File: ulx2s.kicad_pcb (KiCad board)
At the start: 4 copper layers, 35.6 x 61 mm, 23 parts, among them J1 Conn_01x24, J2 Conn_01x24, J3 Micro_SD_Card_Det, J4 USB_OTG, J5 Conn_01x06, SW1 SW_Push, SW2 SW_Push, SW3 SW_Push, SW4 SW_Push, SW5 SW_Push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

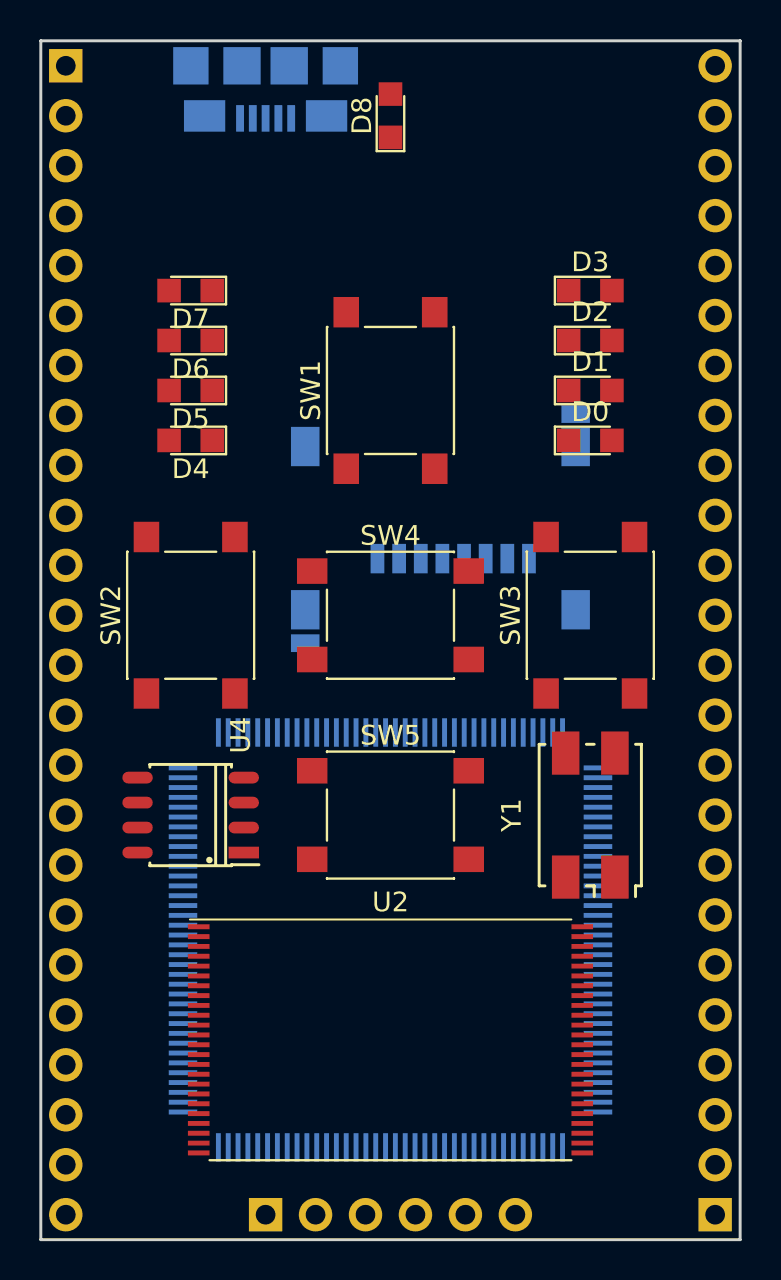
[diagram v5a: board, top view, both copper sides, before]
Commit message: usbserial chip ft232rl
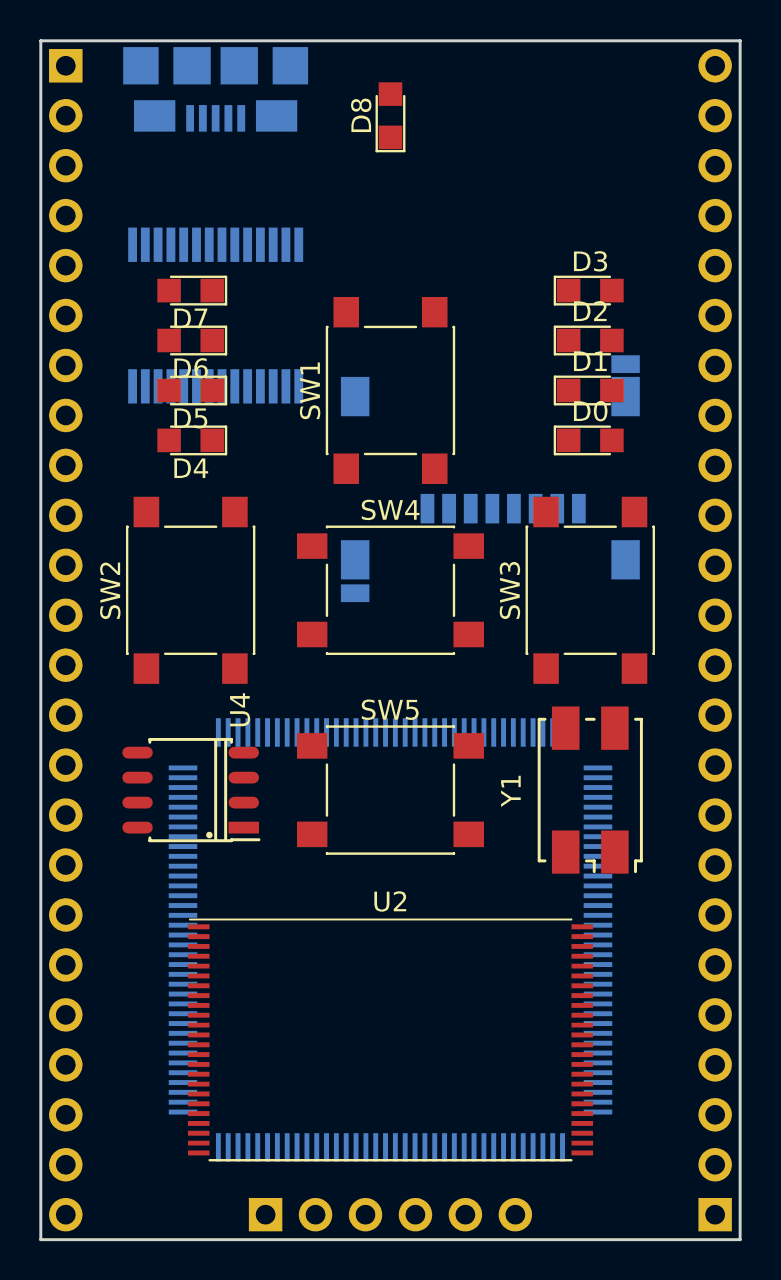
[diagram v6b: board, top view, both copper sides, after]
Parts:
- added U3: FT232RL, Housings_SSOP:SSOP-28_5.3x10.2mm_Pitch0.65mm, B.Cu at (149.9, 95.2)
- moved J3 3.59 mm to (163.8, 102.9)
- moved J4 2.54 mm to (149.9, 82.5)
- moved SW5 1.27 mm to (158.8, 119.4)
- moved U4 1.27 mm to (148.6, 119.4)
- moved Y1 1.27 mm to (168.9, 119.4)
- moved SW2 1.27 mm to (148.6, 109.2)
- moved SW3 1.27 mm to (168.9, 109.2)
- moved SW4 1.27 mm to (158.8, 109.2)
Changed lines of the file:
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@@
     (tracks 0)
     (zones 0)
-    (modules 23)
+    (modules 24)
     (nets 13)
   )
@@
   (layers
     (0 F.Cu signal)
-    (1 In1.Cu signal)
-    (2 In2.Cu signal)
-    (31 B.Cu signal)
+    (1 In1.Cu signal hide)
+    (2 In2.Cu signal hide)
+    (31 B.Cu signal hide)
     (32 B.Adhes user)
     (33 F.Adhes user)
@@
   )
   (module micro-sd:SCHD3A100 (layer B.Cu)
-    (at 161.29 105.41 270)
+    (at 163.83 102.87 270)
     (descr "Micro SD card slot SCHD3A0100 from ALPS or ON-STARS")
     (tags "Micro SD SCHD3A0100")
@@
   )
   (module usb_otg:USB-MICRO-B-FCI-10118192-0001LF (layer B.Cu)
-    (at 152.4 82.55)
+    (at 149.86 82.55)
     (fp_text reference J4 (at 0 4.2) (layer B.SilkS)
       (effects (font (size 0.7 0.7) (thickness 0.15)) (justify mirror))
@@
   )
   (module oscxo:Crystal_SMD_7050_4Pads (layer F.Cu)
-    (at 168.91 120.65 90)
+    (at 168.91 119.38 90)
     (descr "Crystal oscillator, 7.0x5.0mm, 4 Pads")
     (tags "crystal oscillator quartz SMD SMT 7050")
@@
   )
   (module Buttons_Switches_SMD:SW_SPST_PTS645 (layer F.Cu)
-    (at 148.59 110.49 90)
+    (at 148.59 109.22 90)
     (descr "C&K Components SPST SMD PTS645 Series 6mm Tact Switch")
     (tags "SPST Button Switch")
@@
   )
   (module Buttons_Switches_SMD:SW_SPST_PTS645 (layer F.Cu)
-    (at 168.91 110.49 90)
+    (at 168.91 109.22 90)
     (descr "C&K Components SPST SMD PTS645 Series 6mm Tact Switch")
     (tags "SPST Button Switch")
@@
   )
   (module Buttons_Switches_SMD:SW_SPST_PTS645 (layer F.Cu)
-    (at 158.75 110.49)
+    (at 158.75 109.22)
     (descr "C&K Components SPST SMD PTS645 Series 6mm Tact Switch")
     (tags "SPST Button Switch")
@@
   )
   (module Buttons_Switches_SMD:SW_SPST_PTS645 (layer F.Cu)
-    (at 158.75 120.65)
+    (at 158.75 119.38)
     (descr "C&K Components SPST SMD PTS645 Series 6mm Tact Switch")
     (tags "SPST Button Switch")
@@
   )
   (module SOA008-150mil:SOA008-150mil (layer F.Cu)
-    (at 148.59 120.65 180)
+    (at 148.59 119.38 180)
     (descr "Cypress SOA008 SOIC-8 150 mil")
     (tags "SOA008 SOIC-8 1.27 150 mil")
@@
       (at (xyz 0 0 0))
       (scale (xyz 1 1 1))
+      (rotate (xyz 0 0 0))
+    )
+  )
+  (module Housings_SSOP:SSOP-28_5.3x10.2mm_Pitch0.65mm (layer B.Cu)
+    (at 149.86 95.25 90)
+    (descr "28-Lead Plastic Shrink Small Outline (SS)-5.30 mm Body [SSOP] (see Microchip Packaging Specification 00000049BS.pdf)")
+    (tags "SSOP 0.65")
+    (attr smd)
+    (fp_text reference U3 (at 0 6.25 90) (layer B.SilkS)
+      (effects (font (size 1 1) (thickness 0.15)) (justify mirror))
+    )
+    (fp_text value FT232RL (at 0 -6.25 90) (layer B.Fab)
+      (effects (font (size 1 1) (thickness 0.15)) (justify mirror))
+    )
+    (fp_line (start -1.65 5.1) (end 2.65 5.1) (layer B.Fab) (width 0.15))
+    (fp_line (start 2.65 5.1) (end 2.65 -5.1) (layer B.Fab) (width 0.15))
+    (fp_line (start 2.65 -5.1) (end -2.65 -5.1) (layer B.Fab) (width 0.15))
+    (fp_line (start -2.65 -5.1) (end -2.65 4.1) (layer B.Fab) (width 0.15))
+    (fp_line (start -2.65 4.1) (end -1.65 5.1) (layer B.Fab) (width 0.15))
+    (fp_line (start -4.75 5.5) (end -4.75 -5.5) (layer B.CrtYd) (width 0.05))
+    (fp_line (start 4.75 5.5) (end 4.75 -5.5) (layer B.CrtYd) (width 0.05))
+    (fp_line (start -4.75 5.5) (end 4.75 5.5) (layer B.CrtYd) (width 0.05))
+    (fp_line (start -4.75 -5.5) (end 4.75 -5.5) (layer B.CrtYd) (width 0.05))
+    (fp_line (start -2.875 5.325) (end -2.875 4.75) (layer B.SilkS) (width 0.15))
+    (fp_line (start 2.875 5.325) (end 2.875 4.675) (layer B.SilkS) (width 0.15))
+    (fp_line (start 2.875 -5.325) (end 2.875 -4.675) (layer B.SilkS) (width 0.15))
+    (fp_line (start -2.875 -5.325) (end -2.875 -4.675) (layer B.SilkS) (width 0.15))
+    (fp_line (start -2.875 5.325) (end 2.875 5.325) (layer B.SilkS) (width 0.15))
+    (fp_line (start -2.875 -5.325) (end 2.875 -5.325) (layer B.SilkS) (width 0.15))
+    (fp_line (start -2.875 4.75) (end -4.475 4.75) (layer B.SilkS) (width 0.15))
+    (fp_text user %R (at 0 0 90) (layer B.Fab)
+      (effects (font (size 0.8 0.8) (thickness 0.15)) (justify mirror))
+    )
+    (pad 1 smd rect (at -3.6 4.225 90) (size 1.75 0.45) (layers B.Cu B.Paste B.Mask))
+    (pad 2 smd rect (at -3.6 3.575 90) (size 1.75 0.45) (layers B.Cu B.Paste B.Mask))
+    (pad 3 smd rect (at -3.6 2.925 90) (size 1.75 0.45) (layers B.Cu B.Paste B.Mask))
+    (pad 4 smd rect (at -3.6 2.275 90) (size 1.75 0.45) (layers B.Cu B.Paste B.Mask))
+    (pad 5 smd rect (at -3.6 1.625 90) (size 1.75 0.45) (layers B.Cu B.Paste B.Mask))
+    (pad 6 smd rect (at -3.6 0.975 90) (size 1.75 0.45) (layers B.Cu B.Paste B.Mask))
+    (pad 7 smd rect (at -3.6 0.325 90) (size 1.75 0.45) (layers B.Cu B.Paste B.Mask))
+    (pad 8 smd rect (at -3.6 -0.325 90) (size 1.75 0.45) (layers B.Cu B.Paste B.Mask))
+    (pad 9 smd rect (at -3.6 -0.975 90) (size 1.75 0.45) (layers B.Cu B.Paste B.Mask))
+    (pad 10 smd rect (at -3.6 -1.625 90) (size 1.75 0.45) (layers B.Cu B.Paste B.Mask))
+    (pad 11 smd rect (at -3.6 -2.275 90) (size 1.75 0.45) (layers B.Cu B.Paste B.Mask))
+    (pad 12 smd rect (at -3.6 -2.925 90) (size 1.75 0.45) (layers B.Cu B.Paste B.Mask))
+    (pad 13 smd rect (at -3.6 -3.575 90) (size 1.75 0.45) (layers B.Cu B.Paste B.Mask))
+    (pad 14 smd rect (at -3.6 -4.225 90) (size 1.75 0.45) (layers B.Cu B.Paste B.Mask))
+    (pad 15 smd rect (at 3.6 -4.225 90) (size 1.75 0.45) (layers B.Cu B.Paste B.Mask))
+    (pad 16 smd rect (at 3.6 -3.575 90) (size 1.75 0.45) (layers B.Cu B.Paste B.Mask))
+    (pad 17 smd rect (at 3.6 -2.925 90) (size 1.75 0.45) (layers B.Cu B.Paste B.Mask))
+    (pad 18 smd rect (at 3.6 -2.275 90) (size 1.75 0.45) (layers B.Cu B.Paste B.Mask))
+    (pad 19 smd rect (at 3.6 -1.625 90) (size 1.75 0.45) (layers B.Cu B.Paste B.Mask))
+    (pad 20 smd rect (at 3.6 -0.975 90) (size 1.75 0.45) (layers B.Cu B.Paste B.Mask))
+    (pad 21 smd rect (at 3.6 -0.325 90) (size 1.75 0.45) (layers B.Cu B.Paste B.Mask))
+    (pad 22 smd rect (at 3.6 0.325 90) (size 1.75 0.45) (layers B.Cu B.Paste B.Mask))
+    (pad 23 smd rect (at 3.6 0.975 90) (size 1.75 0.45) (layers B.Cu B.Paste B.Mask))
+    (pad 24 smd rect (at 3.6 1.625 90) (size 1.75 0.45) (layers B.Cu B.Paste B.Mask))
+    (pad 25 smd rect (at 3.6 2.275 90) (size 1.75 0.45) (layers B.Cu B.Paste B.Mask))
+    (pad 26 smd rect (at 3.6 2.925 90) (size 1.75 0.45) (layers B.Cu B.Paste B.Mask))
+    (pad 27 smd rect (at 3.6 3.575 90) (size 1.75 0.45) (layers B.Cu B.Paste B.Mask))
+    (pad 28 smd rect (at 3.6 4.225 90) (size 1.75 0.45) (layers B.Cu B.Paste B.Mask))
+    (model ${KISYS3DMOD}/Housings_SSOP.3dshapes/SSOP-28_5.3x10.2mm_Pitch0.65mm.wrl
+      (at (xyz 0 0 0))
+      (scale (xyz 1 1 1))

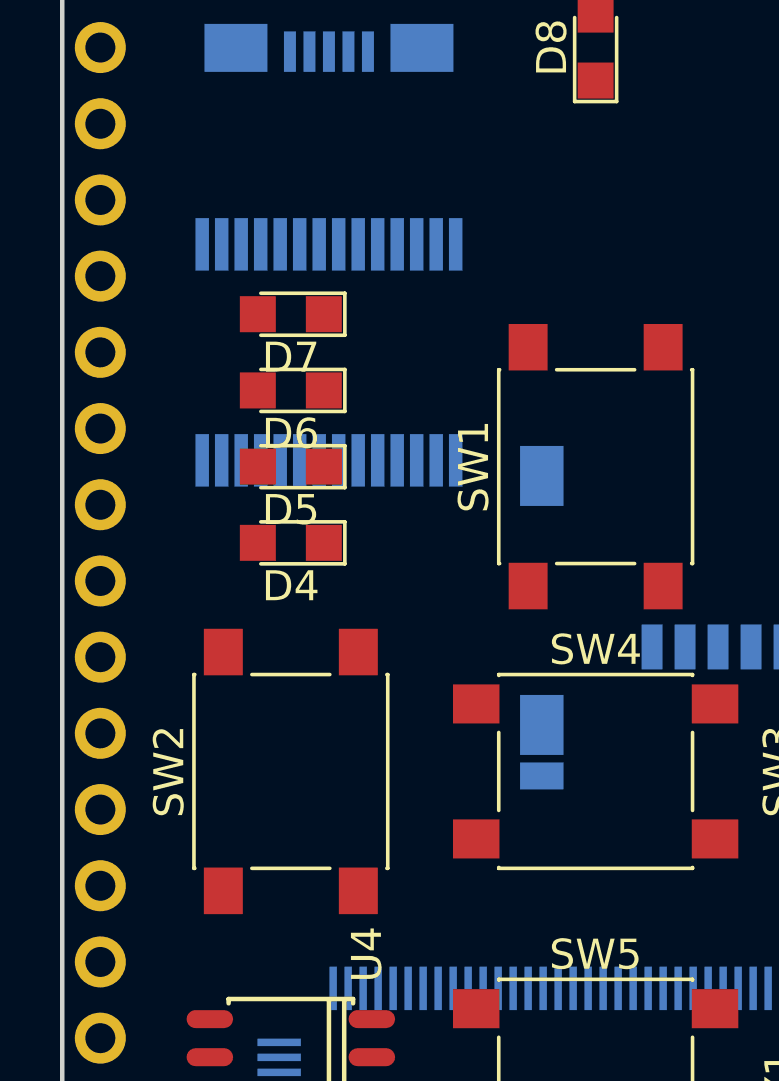
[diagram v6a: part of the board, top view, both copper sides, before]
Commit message: voltage regulators
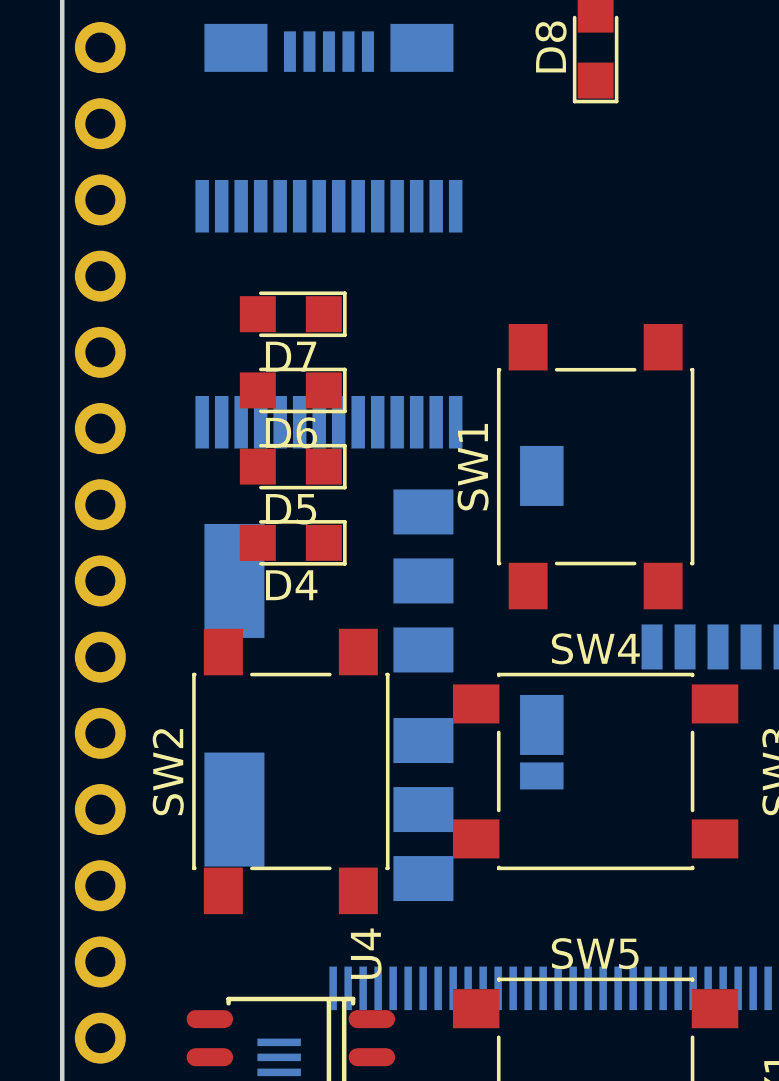
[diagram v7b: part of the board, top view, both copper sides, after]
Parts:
- added U5: AZ1117-3.3, TO_SOT_Packages_SMD:SOT-223, B.Cu at (149.9, 102.9)
- added U6: AZ1117-1.2, TO_SOT_Packages_SMD:SOT-223, B.Cu at (149.9, 110.5)
- moved U3 1.27 mm to (149.9, 94.0)
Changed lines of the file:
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@@
     (tracks 0)
     (zones 0)
-    (modules 24)
+    (modules 26)
     (nets 13)
   )
@@
   )
   (module Housings_SSOP:SSOP-28_5.3x10.2mm_Pitch0.65mm (layer B.Cu)
-    (at 149.86 95.25 90)
+    (at 149.86 93.98 90)
     (descr "28-Lead Plastic Shrink Small Outline (SS)-5.30 mm Body [SSOP] (see Microchip Packaging Specification 00000049BS.pdf)")
     (tags "SSOP 0.65")
@@
       (at (xyz 0 0 0))
       (scale (xyz 1 1 1))
+      (rotate (xyz 0 0 0))
+    )
+  )
+  (module TO_SOT_Packages_SMD:SOT-223 (layer B.Cu)
+    (at 149.86 102.87 180)
+    (descr "module CMS SOT223 4 pins")
+    (tags "CMS SOT")
+    (attr smd)
+    (fp_text reference U5 (at -5.715 0 180) (layer B.SilkS)
+      (effects (font (size 1 1) (thickness 0.15)) (justify mirror))
+    )
+    (fp_text value AZ1117-3.3 (at 0 -4.5 180) (layer B.Fab)
+      (effects (font (size 1 1) (thickness 0.15)) (justify mirror))
+    )
+    (fp_text user %R (at 0 0 450) (layer B.Fab)
+      (effects (font (size 0.8 0.8) (thickness 0.12)) (justify mirror))
+    )
+    (fp_line (start -1.85 2.3) (end -0.8 3.35) (layer B.Fab) (width 0.1))
+    (fp_line (start 1.91 -3.41) (end 1.91 -2.15) (layer B.SilkS) (width 0.12))
+    (fp_line (start 1.91 3.41) (end 1.91 2.15) (layer B.SilkS) (width 0.12))
+    (fp_line (start 4.4 3.6) (end -4.4 3.6) (layer B.CrtYd) (width 0.05))
+    (fp_line (start 4.4 -3.6) (end 4.4 3.6) (layer B.CrtYd) (width 0.05))
+    (fp_line (start -4.4 -3.6) (end 4.4 -3.6) (layer B.CrtYd) (width 0.05))
+    (fp_line (start -4.4 3.6) (end -4.4 -3.6) (layer B.CrtYd) (width 0.05))
+    (fp_line (start -1.85 2.3) (end -1.85 -3.35) (layer B.Fab) (width 0.1))
+    (fp_line (start -1.85 -3.41) (end 1.91 -3.41) (layer B.SilkS) (width 0.12))
+    (fp_line (start -0.8 3.35) (end 1.85 3.35) (layer B.Fab) (width 0.1))
+    (fp_line (start -4.1 3.41) (end 1.91 3.41) (layer B.SilkS) (width 0.12))
+    (fp_line (start -1.85 -3.35) (end 1.85 -3.35) (layer B.Fab) (width 0.1))
+    (fp_line (start 1.85 3.35) (end 1.85 -3.35) (layer B.Fab) (width 0.1))
+    (pad 4 smd rect (at 3.15 0 180) (size 2 3.8) (layers B.Cu B.Paste B.Mask))
+    (pad 2 smd rect (at -3.15 0 180) (size 2 1.5) (layers B.Cu B.Paste B.Mask))
+    (pad 3 smd rect (at -3.15 -2.3 180) (size 2 1.5) (layers B.Cu B.Paste B.Mask))
+    (pad 1 smd rect (at -3.15 2.3 180) (size 2 1.5) (layers B.Cu B.Paste B.Mask))
+    (model ${KISYS3DMOD}/TO_SOT_Packages_SMD.3dshapes/SOT-223.wrl
+      (at (xyz 0 0 0))
+      (scale (xyz 1 1 1))
+      (rotate (xyz 0 0 0))
+    )
+  )
+  (module TO_SOT_Packages_SMD:SOT-223 (layer B.Cu)
+    (at 149.86 110.49 180)
+    (descr "module CMS SOT223 4 pins")
+    (tags "CMS SOT")
+    (attr smd)
+    (fp_text reference U6 (at -5.715 0 180) (layer B.SilkS)
+      (effects (font (size 1 1) (thickness 0.15)) (justify mirror))
+    )
+    (fp_text value AZ1117-1.2 (at 0 -4.5 180) (layer B.Fab)
+      (effects (font (size 1 1) (thickness 0.15)) (justify mirror))
+    )
+    (fp_text user %R (at 0 0 450) (layer B.Fab)
+      (effects (font (size 0.8 0.8) (thickness 0.12)) (justify mirror))
+    )
+    (fp_line (start -1.85 2.3) (end -0.8 3.35) (layer B.Fab) (width 0.1))
+    (fp_line (start 1.91 -3.41) (end 1.91 -2.15) (layer B.SilkS) (width 0.12))
+    (fp_line (start 1.91 3.41) (end 1.91 2.15) (layer B.SilkS) (width 0.12))
+    (fp_line (start 4.4 3.6) (end -4.4 3.6) (layer B.CrtYd) (width 0.05))
+    (fp_line (start 4.4 -3.6) (end 4.4 3.6) (layer B.CrtYd) (width 0.05))
+    (fp_line (start -4.4 -3.6) (end 4.4 -3.6) (layer B.CrtYd) (width 0.05))
+    (fp_line (start -4.4 3.6) (end -4.4 -3.6) (layer B.CrtYd) (width 0.05))
+    (fp_line (start -1.85 2.3) (end -1.85 -3.35) (layer B.Fab) (width 0.1))
+    (fp_line (start -1.85 -3.41) (end 1.91 -3.41) (layer B.SilkS) (width 0.12))
+    (fp_line (start -0.8 3.35) (end 1.85 3.35) (layer B.Fab) (width 0.1))
+    (fp_line (start -4.1 3.41) (end 1.91 3.41) (layer B.SilkS) (width 0.12))
+    (fp_line (start -1.85 -3.35) (end 1.85 -3.35) (layer B.Fab) (width 0.1))
+    (fp_line (start 1.85 3.35) (end 1.85 -3.35) (layer B.Fab) (width 0.1))
+    (pad 4 smd rect (at 3.15 0 180) (size 2 3.8) (layers B.Cu B.Paste B.Mask))
+    (pad 2 smd rect (at -3.15 0 180) (size 2 1.5) (layers B.Cu B.Paste B.Mask))
+    (pad 3 smd rect (at -3.15 -2.3 180) (size 2 1.5) (layers B.Cu B.Paste B.Mask))
+    (pad 1 smd rect (at -3.15 2.3 180) (size 2 1.5) (layers B.Cu B.Paste B.Mask))
+    (model ${KISYS3DMOD}/TO_SOT_Packages_SMD.3dshapes/SOT-223.wrl
+      (at (xyz 0 0 0))
+      (scale (xyz 1 1 1))
